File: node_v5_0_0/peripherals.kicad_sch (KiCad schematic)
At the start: 26 parts, among them U11 1042240820, U12 CAT24M01W, U6 RFM69HCW, U7 PCF8523T, U9 SIM7080G

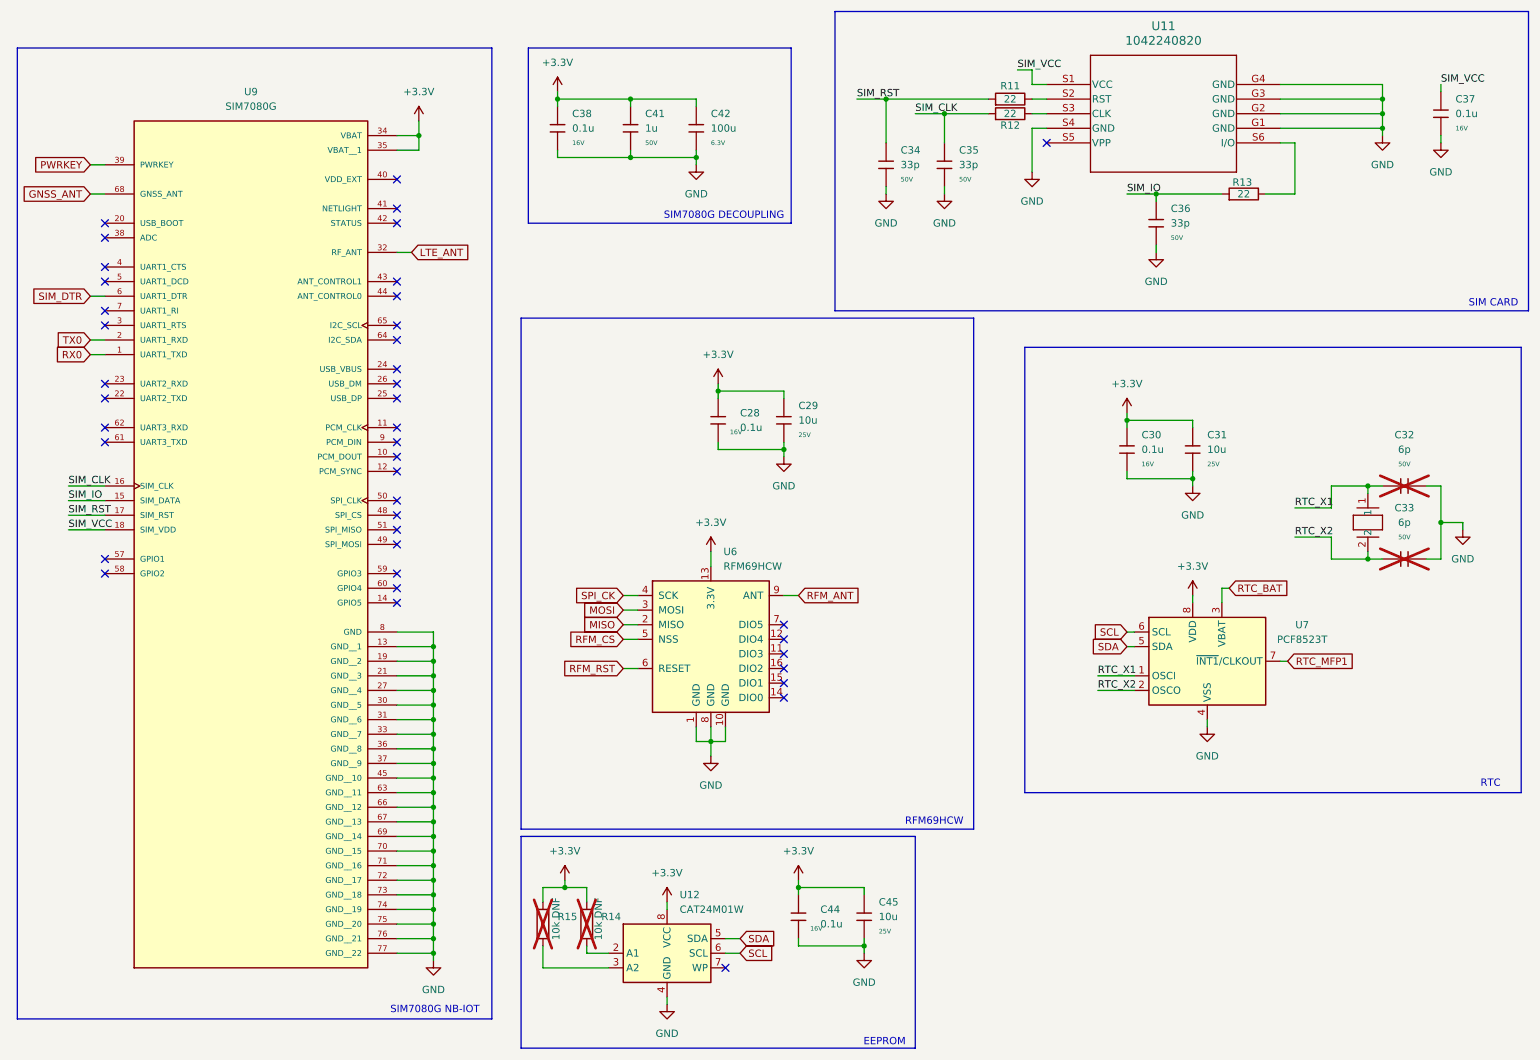
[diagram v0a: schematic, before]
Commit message: updated layout
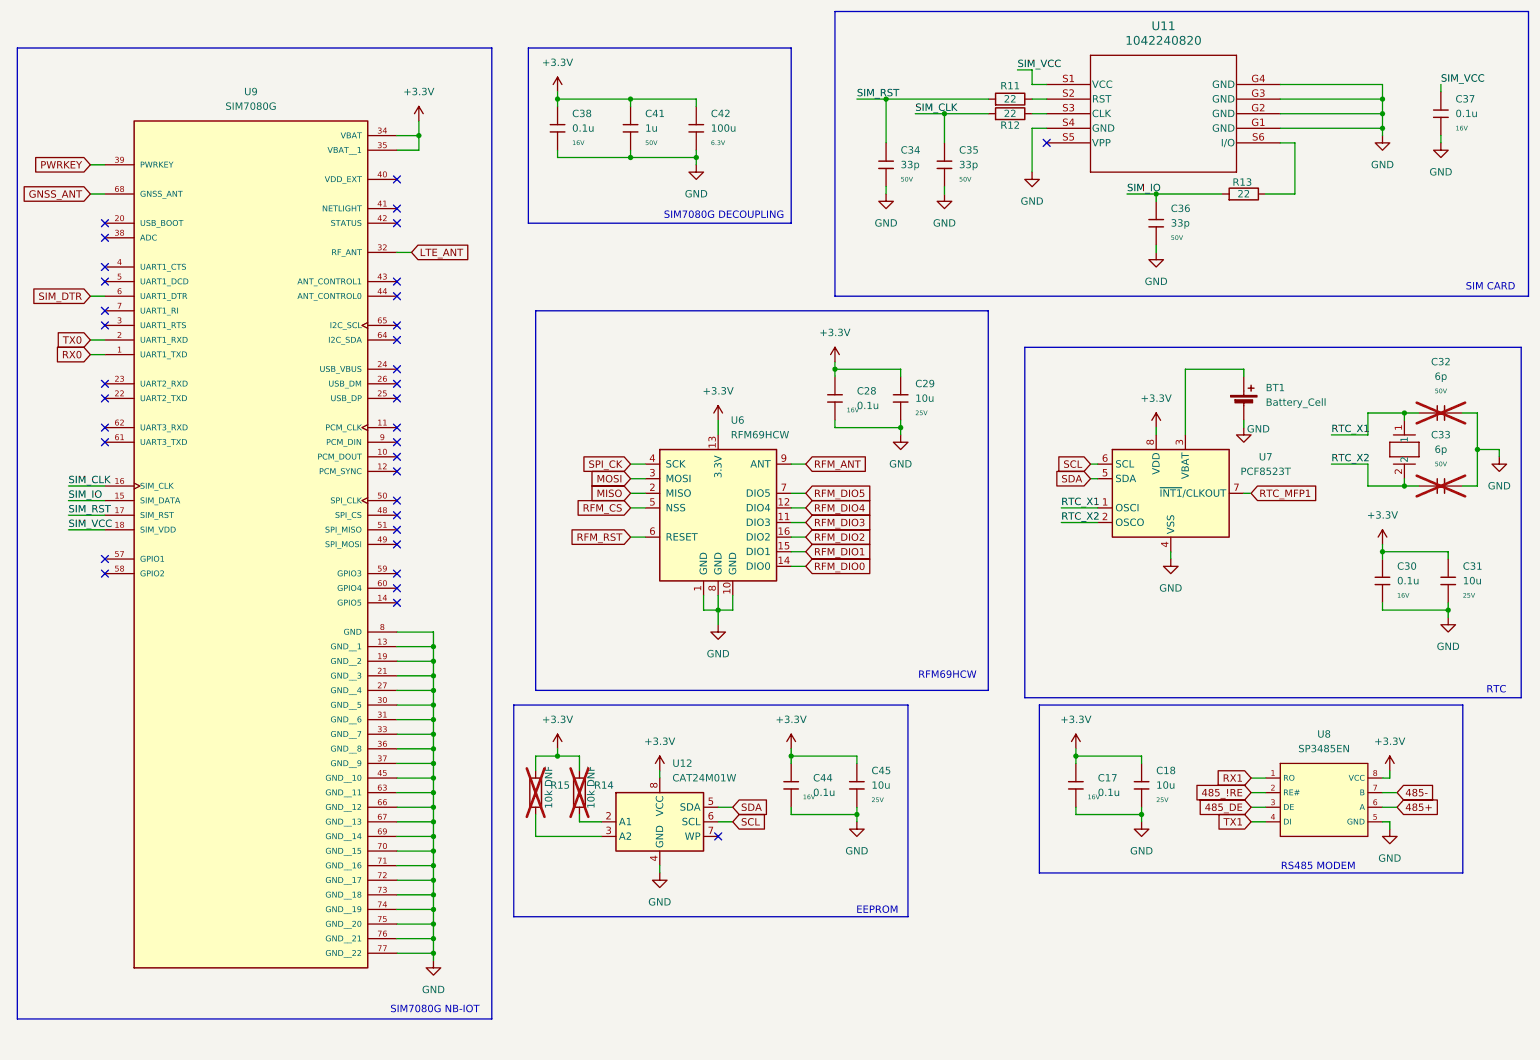
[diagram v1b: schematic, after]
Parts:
- added BT1: Battery_Cell, WiSDOM:BAT_BAT-HLD-001-THM, symbol Device:Battery_Cell
- added C17: 0.1u, JLCPCB-Kicad-Footprints:C_0402, symbol JLCPCB-Capacitors:0402,100nF
- added C18: 10u, JLCPCB-Kicad-Footprints:C_0805, symbol JLCPCB-Capacitors:0805,10uF
- added U8: SP3485EN, JLCPCB-Kicad-Footprints:SOIC-8_L5.0-W4.0-P1.27-LS6.0-BL, symbol JLCPCB-Interface:Transceiver, RS485/422, 10Mbps, SP3485EN-L/TR
- R11, R12, R13: footprint JLCPCB-Kicad-Footprints:R_0805 -> JLCPCB-Kicad-Footprints:R_0402; symbol JLCPCB-Resistors:0805,22Ω -> JLCPCB-Resistors:0402,22Ω; LCSC C17561 -> C25092; Overload Voltage (Max) 150V -> 50V; Part 0805W8F220JT5E -> 0402WGF220JTCE; Power(Watts) 125mW -> 62.5mW; Price 0.005USD -> 0.004USD; Stock 579696 -> 2555256
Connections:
- net +3.3V: now also C17.1, C18.1, U8.8 (VCC)
- net GND: now also BT1.2 (-), C17.2, C18.2, U8.5 (GND)
- net RFM_DIO3: now reaches U6.11 (DIO3)
- net RFM_DIO4: now reaches U6.12 (DIO4)
- net RFM_DIO0: now reaches U6.14 (DIO0)
- net RFM_DIO1: now reaches U6.15 (DIO1)
- net RFM_DIO2: now reaches U6.16 (DIO2)
- net RFM_DIO5: now reaches U6.7 (DIO5)
- net RTC_BAT: no longer names the net of U7.3 (VBAT)
- net RTC_BAT: now also BT1.1 (+)
- new net 485+: U8.6 (A)
- new net 485-: U8.7 (B)
- new net 485_!RE: U8.2 (RE#)
- new net 485_DE: U8.3 (DE)
- new net RX1: U8.1 (RO)
- new net TX1: U8.4 (DI)
- no-connect marks 41 -> 35
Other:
- note added: "RS485 MODEM"
- moved on the sheet: C28, C29, C30, C31, C32, C33, C44, C45, R14, R15, U12, U6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
